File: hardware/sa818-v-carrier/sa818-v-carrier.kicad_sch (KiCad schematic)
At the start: 9 parts, among them J13 Conn_Coaxial, J14 Power/Audio, J15 Control/Data, J16 Conn_01x03_Pin, J17 Conn_01x03_Pin, U9 SA818V

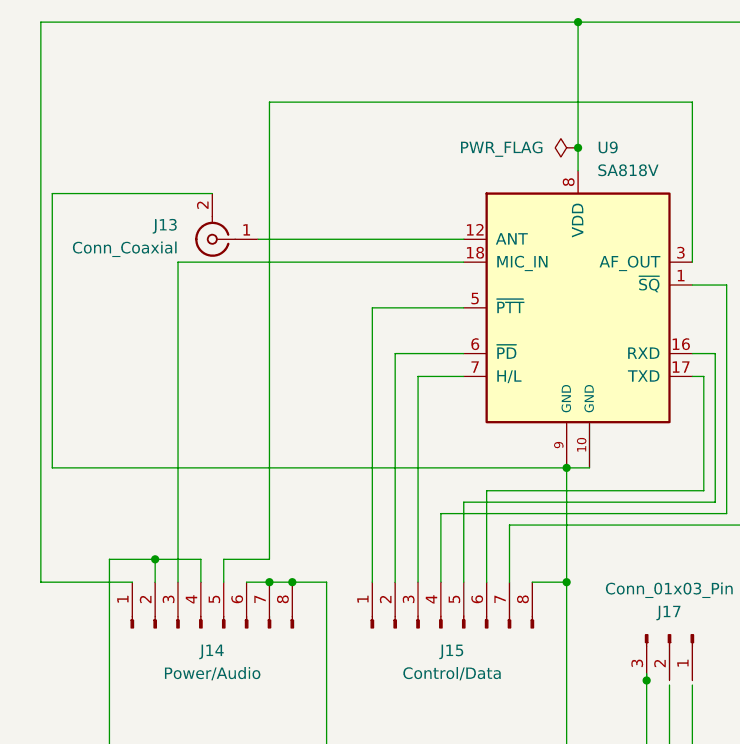
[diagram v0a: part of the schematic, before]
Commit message: add footprints and break carrier boards out into standalone projects
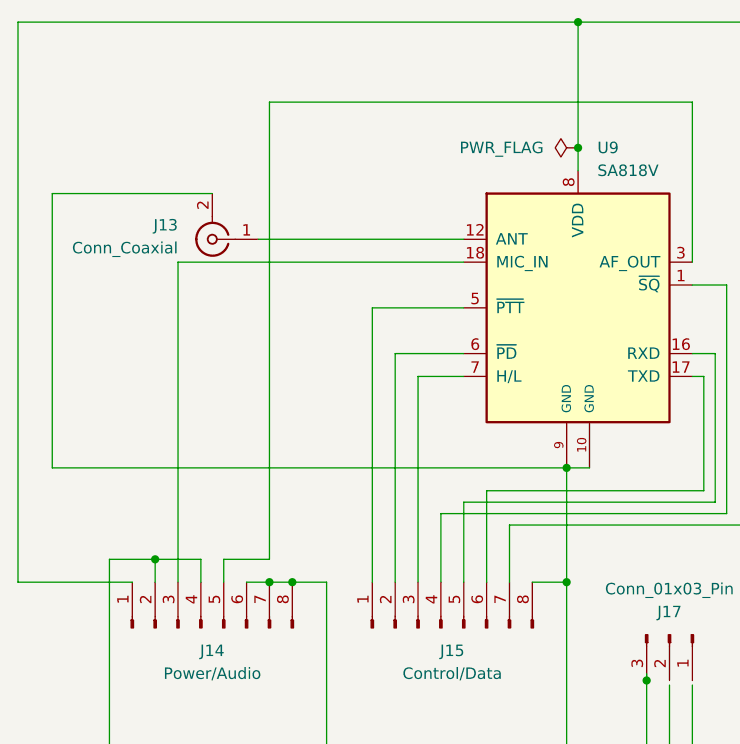
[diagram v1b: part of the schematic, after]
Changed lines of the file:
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@@
 	(wire
 		(pts
-			(xy 147.32 43.18) (xy 87.63 43.18)
+			(xy 147.32 43.18) (xy 85.09 43.18)
 		)
 		(stroke
@@
 	(wire
 		(pts
-			(xy 87.63 43.18) (xy 87.63 105.41)
+			(xy 85.09 43.18) (xy 85.09 105.41)
 		)
 		(stroke
@@
 	(wire
 		(pts
-			(xy 87.63 105.41) (xy 97.79 105.41)
+			(xy 85.09 105.41) (xy 97.79 105.41)
 		)
 		(stroke
@@
 		)
 		(instances
-			(project ""
-				(path "/6bfeada4-0da3-4bdd-af4a-70929e466b35/13b51c95-a7d4-458a-be44-da0982b5e764"
+			(project "sa818-v-carrier"
+				(path "/722b1e9e-d60d-4a57-9f35-4881faa3fde3"
 					(reference "R18")
 					(unit 1)
@@
 		)
 		(instances
-			(project "defcon-sstv-badge"
-				(path "/6bfeada4-0da3-4bdd-af4a-70929e466b35/13b51c95-a7d4-458a-be44-da0982b5e764"
+			(project "sa818-v-carrier"
+				(path "/722b1e9e-d60d-4a57-9f35-4881faa3fde3"
 					(reference "J17")
 					(unit 1)
@@
 		)
 		(instances
-			(project ""
-				(path "/6bfeada4-0da3-4bdd-af4a-70929e466b35/13b51c95-a7d4-458a-be44-da0982b5e764"
+			(project "sa818-v-carrier"
+				(path "/722b1e9e-d60d-4a57-9f35-4881faa3fde3"
 					(reference "#FLG03")
 					(unit 1)
@@
 		)
 		(instances
-			(project ""
-				(path "/6bfeada4-0da3-4bdd-af4a-70929e466b35/13b51c95-a7d4-458a-be44-da0982b5e764"
+			(project "sa818-v-carrier"
+				(path "/722b1e9e-d60d-4a57-9f35-4881faa3fde3"
 					(reference "J15")
 					(unit 1)
@@
 		)
 		(instances
-			(project ""
-				(path "/6bfeada4-0da3-4bdd-af4a-70929e466b35/13b51c95-a7d4-458a-be44-da0982b5e764"
+			(project "sa818-v-carrier"
+				(path "/722b1e9e-d60d-4a57-9f35-4881faa3fde3"
 					(reference "C54")
 					(unit 1)
@@
 		)
 		(instances
-			(project ""
-				(path "/6bfeada4-0da3-4bdd-af4a-70929e466b35/13b51c95-a7d4-458a-be44-da0982b5e764"
+			(project "sa818-v-carrier"
+				(path "/722b1e9e-d60d-4a57-9f35-4881faa3fde3"
 					(reference "J14")
 					(unit 1)
@@
 		)
 		(instances
-			(project ""
-				(path "/6bfeada4-0da3-4bdd-af4a-70929e466b35/13b51c95-a7d4-458a-be44-da0982b5e764"
+			(project "sa818-v-carrier"
+				(path "/722b1e9e-d60d-4a57-9f35-4881faa3fde3"
 					(reference "J13")
 					(unit 1)
@@
 		)
 		(instances
-			(project ""
-				(path "/6bfeada4-0da3-4bdd-af4a-70929e466b35/13b51c95-a7d4-458a-be44-da0982b5e764"
+			(project "sa818-v-carrier"
+				(path "/722b1e9e-d60d-4a57-9f35-4881faa3fde3"
 					(reference "#PWR015")
 					(unit 1)
@@
 		)
 		(instances
-			(project "defcon-sstv-badge"
-				(path "/6bfeada4-0da3-4bdd-af4a-70929e466b35/13b51c95-a7d4-458a-be44-da0982b5e764"
+			(project "sa818-v-carrier"
+				(path "/722b1e9e-d60d-4a57-9f35-4881faa3fde3"
 					(reference "C55")
 					(unit 1)
@@
 		)
 		(instances
-			(project ""
-				(path "/6bfeada4-0da3-4bdd-af4a-70929e466b35/13b51c95-a7d4-458a-be44-da0982b5e764"
+			(project "sa818-v-carrier"
+				(path "/722b1e9e-d60d-4a57-9f35-4881faa3fde3"
 					(reference "U9")
 					(unit 1)
@@
 		)
 		(instances
-			(project ""
-				(path "/6bfeada4-0da3-4bdd-af4a-70929e466b35/13b51c95-a7d4-458a-be44-da0982b5e764"
+			(project "sa818-v-carrier"
+				(path "/722b1e9e-d60d-4a57-9f35-4881faa3fde3"
 					(reference "J16")
 					(unit 1)
@@
 		)
 	)
+	(sheet_instances
+		(path "/"
+			(page "1")
+		)
+	)
+	(embedded_fonts no)
 )

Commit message: VHF Carrier Board
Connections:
- net GND: now also J16.3 (Pin_3), J17.1 (Pin_1), J17.2 (Pin_2)
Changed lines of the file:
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@@
+	)
+	(junction
+		(at 173.99 132.08)
+		(diameter 0)
+		(color 0 0 0 0)
+	)
+	(junction
+		(at 160.02 116.332)
+		(diameter 0)
+		(color 0 0 0 0)
 	)
 	(junction
@@
 	)
 	(junction
+		(at 173.99 116.332)
+		(diameter 0)
+		(color 0 0 0 0)
+	)
+	(junction
 		(at 218.44 132.08)
 		(diameter 0)
@@
 	)
 	(junction
+		(at 157.48 116.332)
+		(diameter 0)
+		(color 0 0 0 0)
+	)
+	(junction
 		(at 154.94 132.08)
 		(diameter 0)
@@
 		(color 0 0 0 0)
 	)
-	(junction
-		(at 173.99 132.08)
-		(diameter 0)
-		(color 0 0 0 0)
-	)
 	(wire
 		(pts
@@
 	(wire
 		(pts
+			(xy 173.99 115.57) (xy 173.99 116.332)
+		)
+		(stroke
+			(width 0)
+			(type default)
+		)
+	)
+	(wire
+		(pts
 			(xy 179.07 132.08) (xy 204.47 132.08)
 		)
@@
 	(wire
 		(pts
+			(xy 173.99 132.08) (xy 176.53 132.08)
+		)
+		(stroke
+			(width 0)
+			(type default)
+		)
+	)
+	(wire
+		(pts
 			(xy 233.68 132.08) (xy 218.44 132.08)
 		)
@@
 	(wire
 		(pts
-			(xy 173.99 116.84) (xy 173.99 132.08)
-		)
-		(stroke
-			(width 0)
-			(type default)
-		)
-	)
-	(wire
-		(pts
 			(xy 100.33 102.87) (xy 95.25 102.87)
 		)
@@
 	(wire
 		(pts
-			(xy 157.48 116.84) (xy 157.48 132.08)
+			(xy 157.48 115.57) (xy 157.48 116.332)
 		)
 		(stroke
@@
 	(wire
 		(pts
+			(xy 161.29 82.55) (xy 161.29 95.25)
+		)
+		(stroke
+			(width 0)
+			(type default)
+		)
+	)
+	(wire
+		(pts
+			(xy 161.29 95.25) (xy 137.16 95.25)
+		)
+		(stroke
+			(width 0)
+			(type default)
+		)
+	)
+	(wire
+		(pts
+			(xy 119.38 105.41) (xy 119.38 132.08)
+		)
+		(stroke
+			(width 0)
+			(type default)
+		)
+	)
+	(wire
+		(pts
+			(xy 146.05 105.41) (xy 146.05 132.08)
+		)
+		(stroke
+			(width 0)
+			(type default)
+		)
+	)
+	(wire
+		(pts
+			(xy 146.05 132.08) (xy 154.94 132.08)
+		)
+		(stroke
+			(width 0)
+			(type default)
+		)
+	)
+	(wire
+		(pts
+			(xy 129.54 82.55) (xy 129.54 105.41)
+		)
+		(stroke
+			(width 0)
+			(type default)
+		)
+	)
+	(wire
+		(pts
+			(xy 111.76 67.31) (xy 134.62 67.31)
+		)
+		(stroke
+			(width 0)
+			(type default)
+		)
+	)
+	(wire
+		(pts
+			(xy 233.68 111.76) (xy 233.68 132.08)
+		)
+		(stroke
+			(width 0)
+			(type default)
+		)
+	)
+	(wire
+		(pts
+			(xy 176.53 132.08) (xy 179.07 132.08)
+		)
+		(stroke
+			(width 0)
+			(type default)
+		)
+	)
+	(wire
+		(pts
+			(xy 160.02 116.332) (xy 160.02 132.08)
+		)
+		(stroke
+			(width 0)
+			(type default)
+		)
+	)
+	(wire
+		(pts
+			(xy 162.56 96.52) (xy 134.62 96.52)
+		)
+		(stroke
+			(width 0)
+			(type default)
+		)
+	)
+	(wire
+		(pts
+			(xy 204.47 43.18) (xy 204.47 104.14)
+		)
+		(stroke
+			(width 0)
+			(type default)
+		)
+	)
+	(wire
+		(pts
+			(xy 204.47 43.18) (xy 218.44 43.18)
+		)
+		(stroke
+			(width 0)
+			(type default)
+		)
+	)
+	(wire
+		(pts
+			(xy 160.02 80.01) (xy 162.56 80.01)
+		)
+		(stroke
+			(width 0)
+			(type default)
+		)
+	)
+	(wire
+		(pts
+			(xy 105.41 105.41) (xy 105.41 102.87)
+		)
+		(stroke
+			(width 0)
+			(type default)
+		)
+	)
+	(wire
+		(pts
+			(xy 160.02 72.39) (xy 163.83 72.39)
+		)
+		(stroke
+			(width 0)
+			(type default)
+		)
+	)
+	(wire
+		(pts
+			(xy 179.07 115.57) (xy 179.07 116.332)
+		)
+		(stroke
+			(width 0)
+			(type default)
+		)
+	)
+	(wire
+		(pts
 			(xy 160.02 132.08) (xy 173.99 132.08)
 		)
@@
 	(wire
 		(pts
-			(xy 161.29 82.55) (xy 161.29 95.25)
-		)
-		(stroke
-			(width 0)
-			(type default)
-		)
-	)
-	(wire
-		(pts
-			(xy 161.29 95.25) (xy 137.16 95.25)
-		)
-		(stroke
-			(width 0)
-			(type default)
-		)
-	)
-	(wire
-		(pts
-			(xy 119.38 105.41) (xy 119.38 132.08)
-		)
-		(stroke
-			(width 0)
-			(type default)
-		)
-	)
-	(wire
-		(pts
-			(xy 146.05 105.41) (xy 146.05 132.08)
-		)
-		(stroke
-			(width 0)
-			(type default)
-		)
-	)
-	(wire
-		(pts
-			(xy 146.05 132.08) (xy 154.94 132.08)
-		)
-		(stroke
-			(width 0)
-			(type default)
-		)
-	)
-	(wire
-		(pts
-			(xy 129.54 82.55) (xy 129.54 105.41)
-		)
-		(stroke
-			(width 0)
-			(type default)
-		)
-	)
-	(wire
-		(pts
-			(xy 111.76 67.31) (xy 134.62 67.31)
-		)
-		(stroke
-			(width 0)
-			(type default)
-		)
-	)
-	(wire
-		(pts
-			(xy 233.68 111.76) (xy 233.68 132.08)
-		)
-		(stroke
-			(width 0)
-			(type default)
-		)
-	)
-	(wire
-		(pts
-			(xy 176.53 132.08) (xy 179.07 132.08)
-		)
-		(stroke
-			(width 0)
-			(type default)
-		)
-	)
-	(wire
-		(pts
-			(xy 162.56 96.52) (xy 134.62 96.52)
-		)
-		(stroke
-			(width 0)
-			(type default)
-		)
-	)
-	(wire
-		(pts
-			(xy 204.47 43.18) (xy 204.47 104.14)
-		)
-		(stroke
-			(width 0)
-			(type default)
-		)
-	)
-	(wire
-		(pts
-			(xy 204.47 43.18) (xy 218.44 43.18)
-		)
-		(stroke
-			(width 0)
-			(type default)
-		)
-	)
-	(wire
-		(pts
-			(xy 160.02 80.01) (xy 162.56 80.01)
-		)
-		(stroke
-			(width 0)
-			(type default)
-		)
-	)
-	(wire
-		(pts
-			(xy 105.41 105.41) (xy 105.41 102.87)
-		)
-		(stroke
-			(width 0)
-			(type default)
-		)
-	)
-	(wire
-		(pts
-			(xy 160.02 72.39) (xy 163.83 72.39)
-		)
-		(stroke
-			(width 0)
-			(type default)
-		)
-	)
-	(wire
-		(pts
-			(xy 179.07 115.57) (xy 179.07 116.332)
-		)
-		(stroke
-			(width 0)
-			(type default)
-		)
-	)
-	(wire
-		(pts
-			(xy 173.99 132.08) (xy 176.53 132.08)
-		)
-		(stroke
-			(width 0)
-			(type default)
-		)
-	)
-	(wire
-		(pts
 			(xy 134.62 74.93) (xy 124.46 74.93)
 		)
@@
 	(wire
 		(pts
+			(xy 157.48 116.332) (xy 157.48 132.08)
+		)
+		(stroke
+			(width 0)
+			(type default)
+		)
+	)
+	(wire
+		(pts
 			(xy 134.62 69.85) (xy 102.87 69.85)
 		)
@@
 	(wire
 		(pts
+			(xy 173.99 116.332) (xy 173.99 132.08)
+		)
+		(stroke
+			(width 0)
+			(type default)
+		)
+	)
+	(wire
+		(pts
 			(xy 157.48 132.08) (xy 160.02 132.08)
 		)
@@
 	(wire
 		(pts
-			(xy 160.02 116.84) (xy 160.02 132.08)
-		)
-		(stroke
+			(xy 160.02 115.57) (xy 160.02 116.332)
+		)
+		(stroke

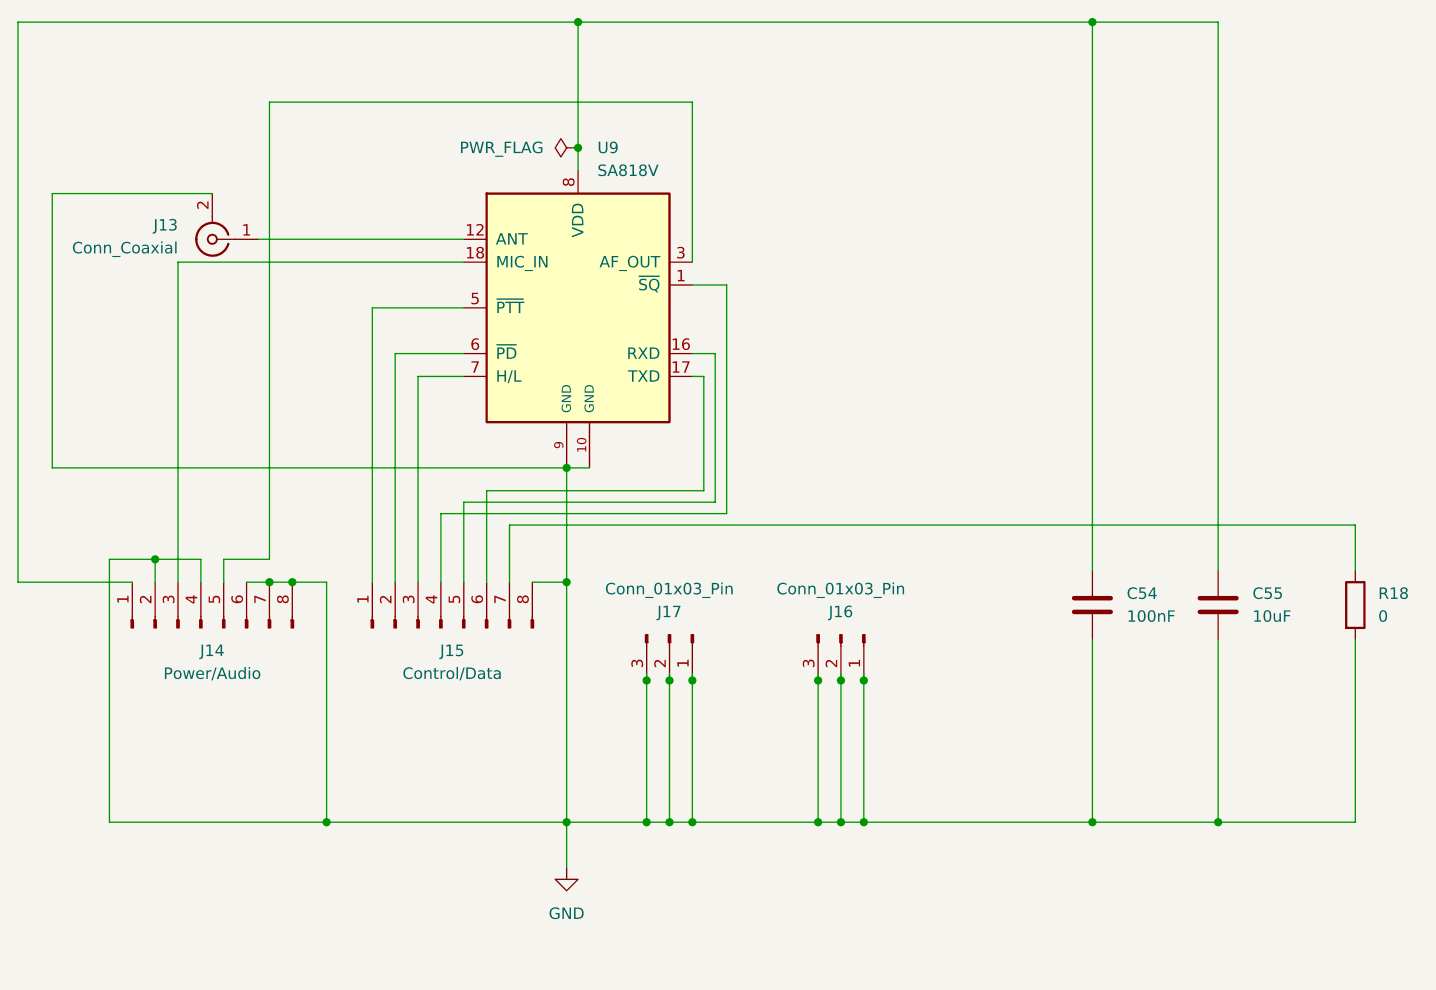
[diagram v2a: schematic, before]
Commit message: routing and component bug fixes
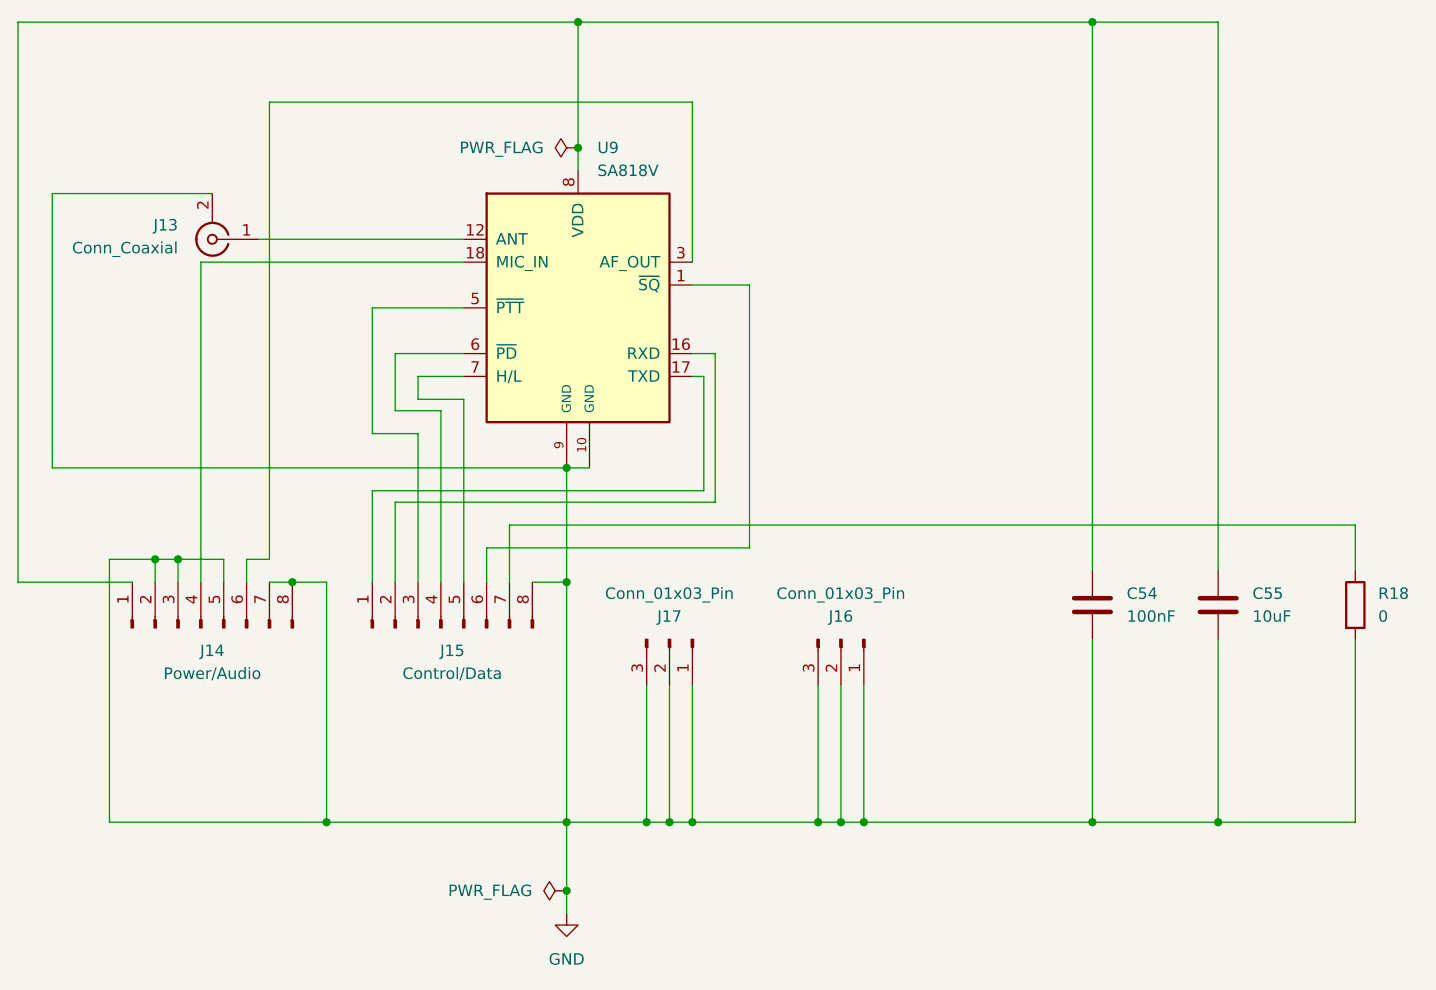
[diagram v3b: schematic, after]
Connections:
- net GND: now also J14.3 (Pin_3), J14.5 (Pin_5); no longer J14.4 (Pin_4), J14.6 (Pin_6)
- net at J15.1 (Pin_1): now also U9.17 (TXD); no longer U9.5 (~{PTT})
- net at J15.2 (Pin_2): now also U9.16 (RXD); no longer U9.6 (~{PD})
- net at J15.3 (Pin_3): now also U9.5 (~{PTT}); no longer U9.7 (H/L)
- net at J15.4 (Pin_4): now also U9.6 (~{PD}); no longer U9.1 (~{SQ})
- net at J15.5 (Pin_5): now also U9.7 (H/L); no longer U9.16 (RXD)
- net at J15.6 (Pin_6): now also U9.1 (~{SQ}); no longer U9.17 (TXD)
- net at U9.18 (MIC_IN): now also J14.4 (Pin_4); no longer J14.3 (Pin_3)
- net at U9.3 (AF_OUT): now also J14.6 (Pin_6); no longer J14.5 (Pin_5)
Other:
- moved on the sheet: J16, J17
